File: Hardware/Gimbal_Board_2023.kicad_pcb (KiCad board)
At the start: 2 copper layers, 72 parts, among them J1 6P6C, J2 RJ45_LED_Shielded, Q1 Q_NMOS_GDS, Q2 Q_NMOS_GDS, Q3 Q_NMOS_GDS, Q4 Q_NMOS_GDS, Q5 Q_NMOS_GDS, Q6 Q_NMOS_GDS, Q7 Q_NMOS_GDS, SW1 SW_Push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

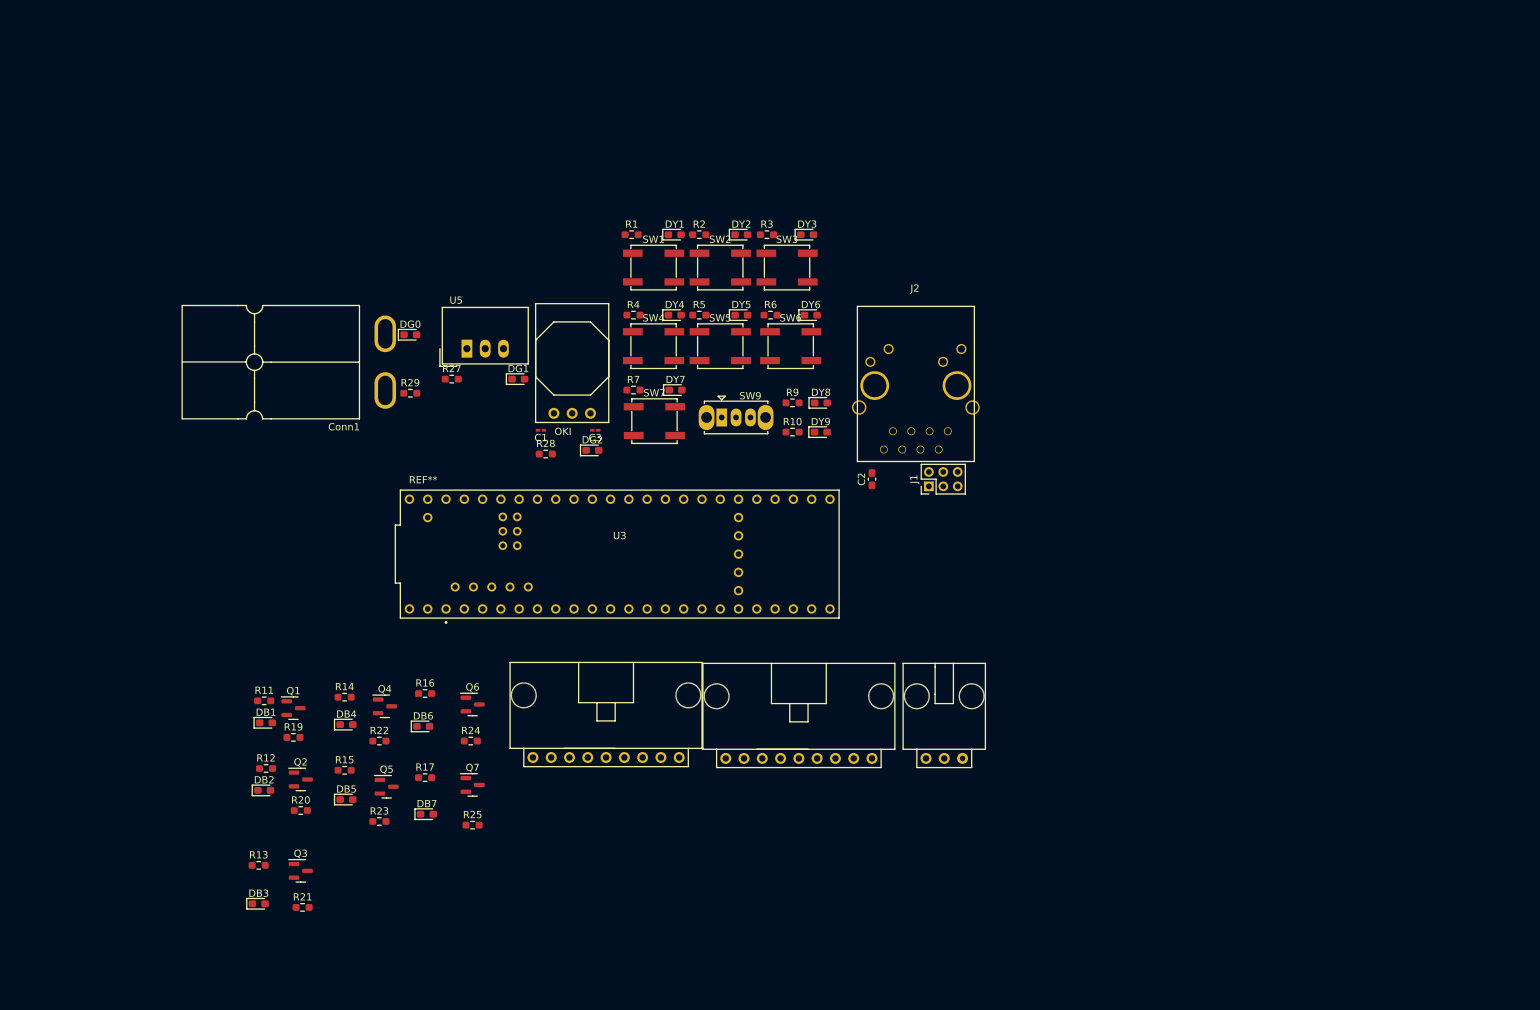
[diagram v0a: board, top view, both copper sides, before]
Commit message: Moved components around and started to wire ethernet
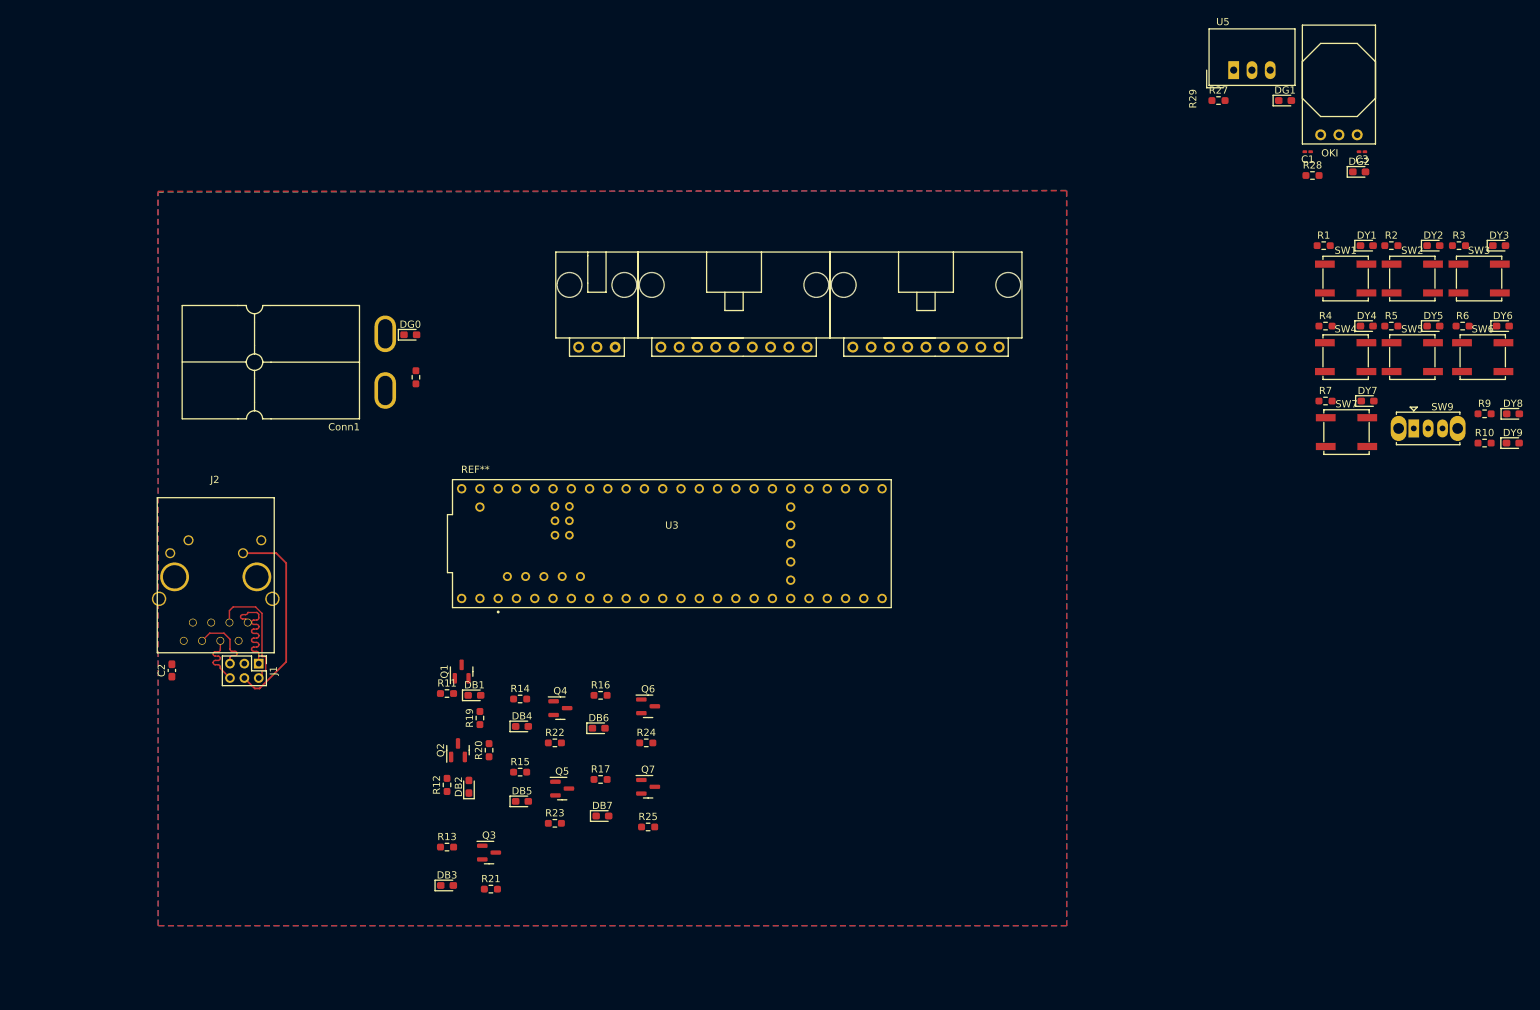
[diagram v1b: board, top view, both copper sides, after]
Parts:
- moved C1 113.3 mm to (233.9, 40.8)
- moved C3 113.3 mm to (241.4, 40.8)
- moved DG2 113.3 mm to (241.0, 43.6)
- moved R28 113.3 mm to (234.5, 44.1)
- moved U1 113.3 mm to (240.8, 38.4)
- moved U5 113.3 mm to (223.6, 29.5)
- moved DG1 113.3 mm to (230.7, 33.7)
- moved R27 113.3 mm to (221.5, 33.7)
- moved C2 100.8 mm to (76.1, 112.9)
- moved J2 100.8 mm to (82.0, 86.9)
- moved J1 96.3 mm to (88.1, 111.9), turned to -90 degrees
- moved DY2 96.2 mm to (251.3, 53.8)
- moved DY5 96.2 mm to (251.3, 65.0)
- moved DY6 96.2 mm to (261.0, 65.0)
- moved DY8 96.2 mm to (262.4, 77.2)
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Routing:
- net /LED: track 0.00 -> 28.2 mm
- net /TX+: track 0.00 -> 17.1 mm
- net /TX-: track 0.00 -> 17.0 mm
- net /RX-: track 0.00 -> 9.50 mm
- net /RX+: track 0.00 -> 8.59 mm
- added copper zone on B.Cu, net +3.3V
- added copper zone on F.Cu, net GND

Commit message: Wire management
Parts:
- moved DY1 169.6 mm to (81.6, 108.7), turned to -90 degrees
- moved DY2 164.8 mm to (95.8, 108.3), turned to 180 degrees
- moved DY3 160.9 mm to (109.0, 108.2), turned to 180 degrees
- moved SW1 160.4 mm to (85.0, 102.7), turned to 180 degrees
- moved R1 158.0 mm to (87.9, 108.5), turned to 90 degrees
- moved SW2 156.1 mm to (98.8, 103.0), turned to 180 degrees
- moved R2 153.8 mm to (101.6, 108.3), turned to 180 degrees
- moved SW3 152.7 mm to (111.6, 102.8), turned to 180 degrees
- moved R3 150.7 mm to (114.4, 108.2), turned to 180 degrees
- moved DY6 146.1 mm to (121.6, 108.5), turned to 180 degrees
- moved SW6 137.9 mm to (124.5, 103.0), turned to 180 degrees
- moved DG1 137.5 mm to (96.2, 61.9)
- moved R6 135.3 mm to (127.3, 108.5), turned to 180 degrees
- moved U5 129.5 mm to (96.9, 56.0)
- moved C3 126.8 mm to (117.3, 67.2), turned to -90 degrees
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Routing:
- net Servo_2_PWM: track 0.00 -> 121.1 mm
- net Servo_1_PWM: track 0.00 -> 112.7 mm, vias 0 -> 2
- net +36V: track 0.08 -> 44.5 mm
- net Servo_6_PWM: track 0.00 -> 34.9 mm, vias 0 -> 2
- net Servo_5_PWM: track 0.00 -> 27.5 mm
- net +3.3V: track 0.00 -> 22.9 mm, vias 0 -> 2
- net Servo_3_PWM: track 0.00 -> 20.2 mm, vias 0 -> 2
- net Servo_1_SW: track 0.00 -> 16.7 mm
- net Net-(C2-Pad1): track 0.00 -> 15.9 mm
- net Servo_Manual_Control_Left: track 0.00 -> 12.9 mm
- net Servo_Manual_Control_Right: track 0.00 -> 11.7 mm
- net Servo_4_PWM: track 0.00 -> 10.1 mm, vias 0 -> 2
- net Servo_3_SW: track 0.00 -> 7.22 mm
- net Net-(DY8-Pad2): track 0.00 -> 7.10 mm
- net Net-(DY1-Pad2): track 0.00 -> 6.40 mm
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- added copper zone on B.Cu, net GND
- removed copper zone on B.Cu, net +3.3V

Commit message: Rearranged and rerouted connections
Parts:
- moved DY6 59.8 mm to (181.4, 109.9), turned to 0 degrees
- moved R6 59.2 mm to (186.4, 109.0), turned to 90 degrees
- moved Q3 58.3 mm to (140.9, 65.1), turned to 90 degrees
- moved Q1 58.2 mm to (113.7, 65.4), turned to 90 degrees
- moved SW6 56.9 mm to (181.4, 102.9)
- moved R21 53.9 mm to (145.5, 68.9), turned to 90 degrees
- moved R19 53.7 mm to (118.4, 69.0)
- moved Conn8 53.6 mm to (184.2, 56.8)
- moved R11 53.6 mm to (113.8, 68.3), turned to 180 degrees
- moved R13 51.8 mm to (141.1, 68.1), turned to 180 degrees
- moved DB3 50.2 mm to (144.5, 66.2), turned to 0 degrees
- moved SW9 50.2 mm to (120.7, 89.9), turned to 0 degrees
- moved DB1 50.0 mm to (117.5, 66.3), turned to 0 degrees
- moved DY8 47.7 mm to (120.8, 79.4), turned to -90 degrees
- moved DY9 46.9 mm to (124.7, 79.5)
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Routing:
- net +5V: track 4.04 -> 192.8 mm, vias 0 -> 10
- net Servo_2_PWM: track 121.1 -> 52.4 mm
- net Servo_7_PWM: track 0.58 -> 62.3 mm
- net +3.3V: track 22.9 -> 81.5 mm, vias 2 -> 0
- net Servo_1_SW: track 16.7 -> 71.7 mm, vias 0 -> 2
- net Servo_2_SW: track 5.76 -> 60.2 mm, vias 0 -> 2
- net Servo_1_PWM: track 112.7 -> 58.6 mm, vias 2 -> 0
- net Servo_3_SW: track 7.22 -> 51.5 mm, vias 0 -> 2
- net Servo_Manual_Control_Left: track 12.9 -> 56.2 mm
- net Servo_4_PWM: track 10.1 -> 47.5 mm, vias 2 -> 0
- net Servo_Manual_Control_Right: track 11.7 -> 48.8 mm
- net Servo_4_SW: track 5.76 -> 39.7 mm, vias 0 -> 2
- net Servo_5_PWM: track 27.5 -> 53.6 mm
- net Servo_5_SW: track 5.76 -> 30.1 mm, vias 0 -> 2
- net Servo_3_PWM: track 20.2 -> 43.9 mm, vias 2 -> 0
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
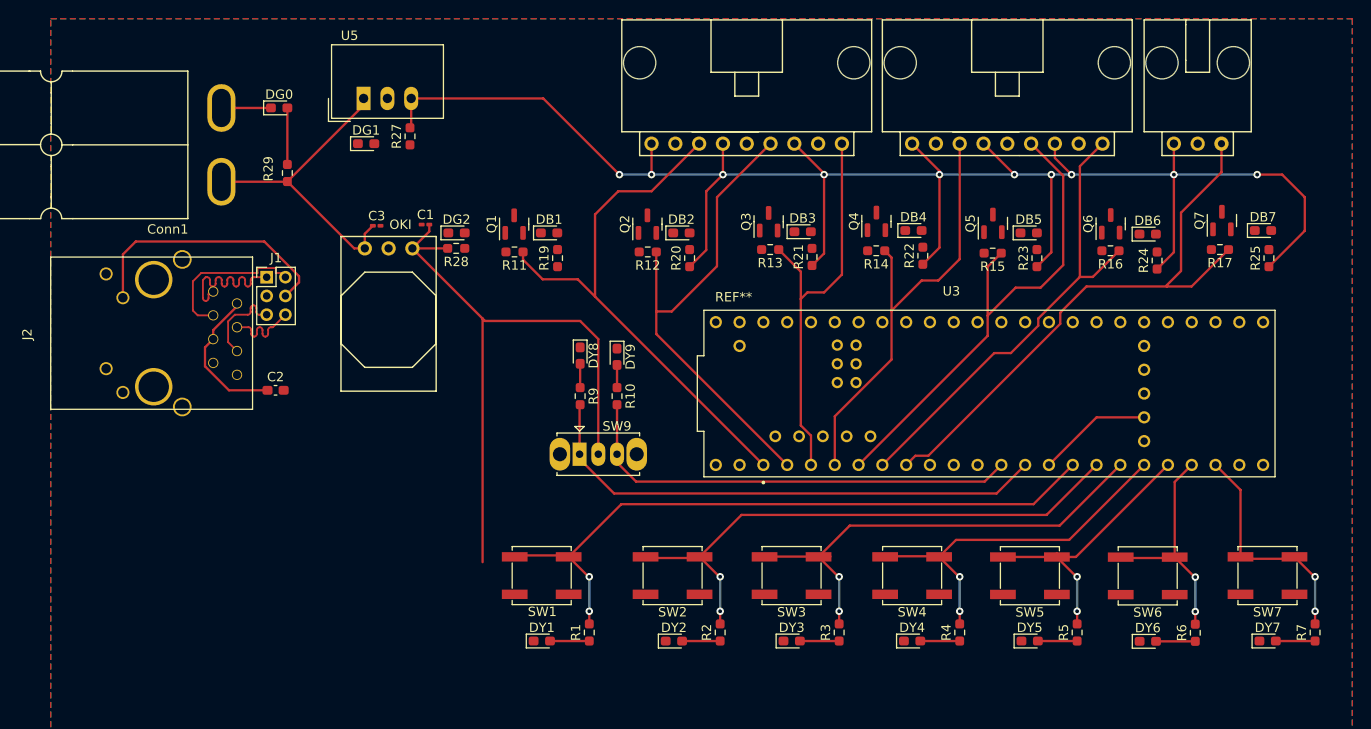
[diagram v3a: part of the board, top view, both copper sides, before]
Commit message: Cable management
Redid ethernet lines to make them closer in length to each other
Ran 3.3 line around bottom
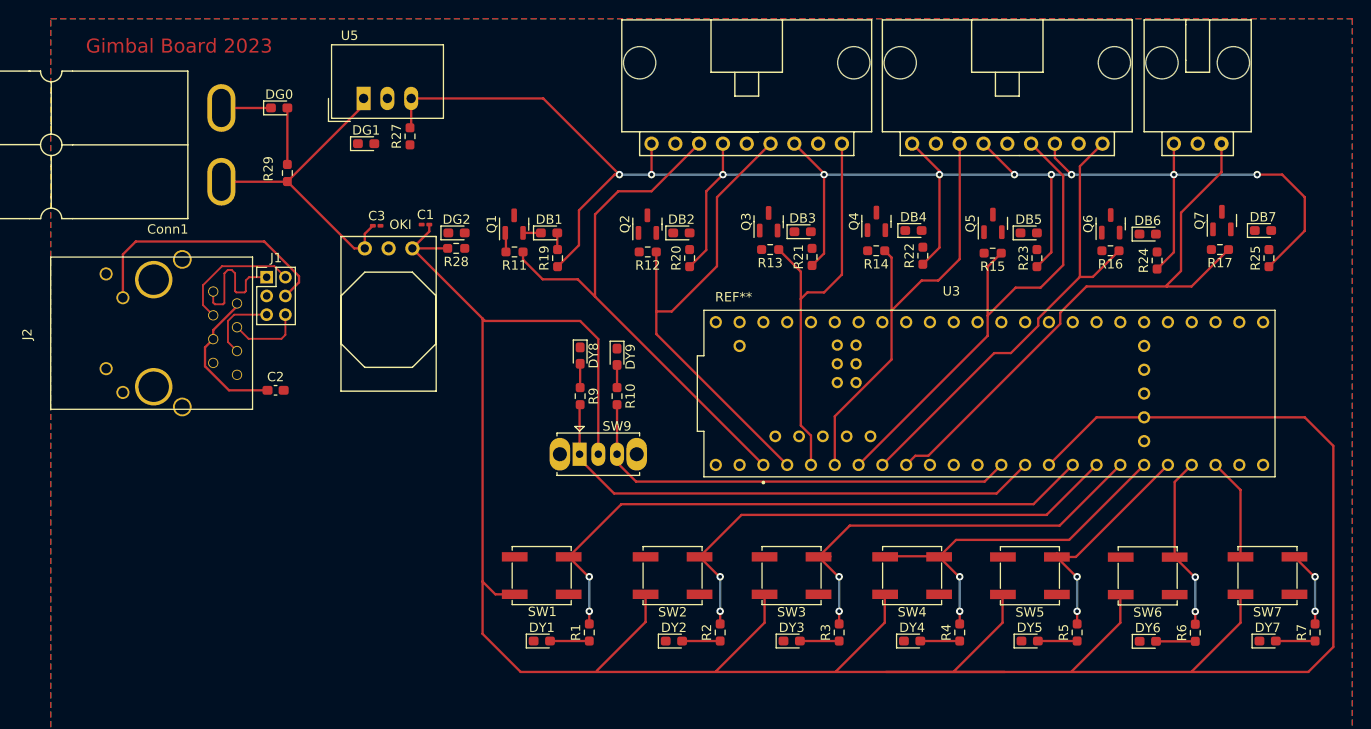
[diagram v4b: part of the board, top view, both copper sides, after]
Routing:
- net +3.3V: track 81.5 -> 304.2 mm
- net +5V: track 192.8 -> 205.6 mm
- net Servo_7_SW: track 24.7 -> 19.0 mm
- net Servo_3_SW: track 51.5 -> 45.8 mm
- net Servo_1_SW: track 71.7 -> 66.0 mm
- net Servo_2_SW: track 60.2 -> 54.5 mm
- net Servo_6_SW: track 24.4 -> 18.6 mm
- net Servo_5_SW: track 30.1 -> 24.4 mm
- net /TX-: track 17.0 -> 13.8 mm
- net /TX+: track 16.6 -> 13.8 mm
- net Net-(Q1-Pad1): track 0.00 -> 2.06 mm
- net Net-(DB1-Pad1): track 0.00 -> 1.91 mm
- net Net-(DB1-Pad2): track 0.00 -> 1.79 mm
- net /RX-: track 9.41 -> 8.02 mm
- net /RX+: track 8.59 -> 8.01 mm
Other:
- board text added: "Gimbal Board 2023"
